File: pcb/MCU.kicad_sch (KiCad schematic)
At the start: 47 parts, among them J3 Conn_ST_STDC14, J4 Micro_SD_Card, SW1 SW_BLUE, SW2 SW_BLACK, U7 STM32U595ZJTx, Y2 16MHz

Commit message: pcb
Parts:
- removed C65, C66, C71: 100nF, Capacitor_SMD:C_0805_2012Metric_Pad1.18x1.45mm_HandSolder, symbol Device:C
- removed C67, C68, C70: 1uF, Capacitor_SMD:C_0805_2012Metric_Pad1.18x1.45mm_HandSolder, symbol Device:C
- renumbered C69 to C65, C72 to C66, C73 to C67, C74 to C68, D4 to D7, J3 to J4, J4 to J5, R37 to R42, R38 to R43, R39 to R44, R40 to R45, R41 to R46, R42 to R47, R43 to R48, R44 to R49, R45 to R50, R47 to R51, R48 to R52, R49 to R53, R50 to R54, R51 to R55, R52 to R56, U7 to U6
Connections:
- net +3V3A is gone; now on net +3V3: U6.32 (VREF+), U6.33 (VDDA)
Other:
- moved on the sheet: C65, SW2

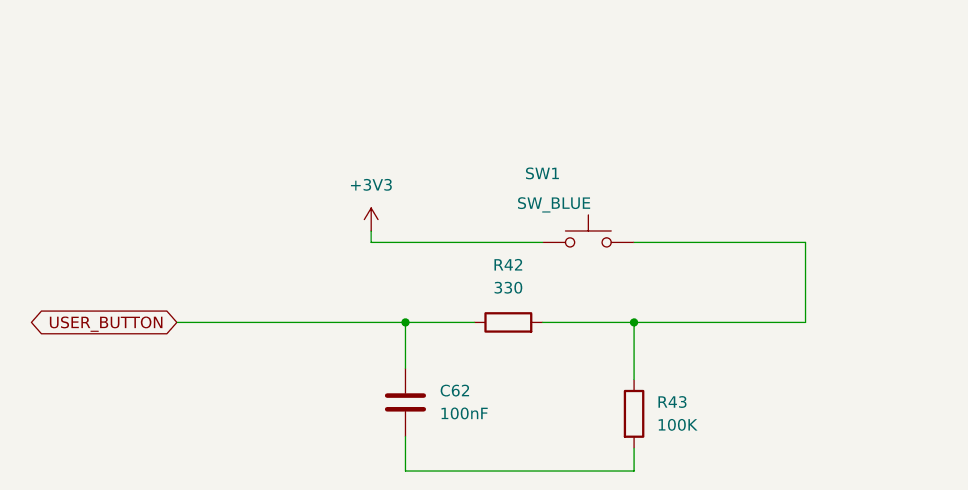
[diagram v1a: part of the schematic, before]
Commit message: pcb: simplify mcu led
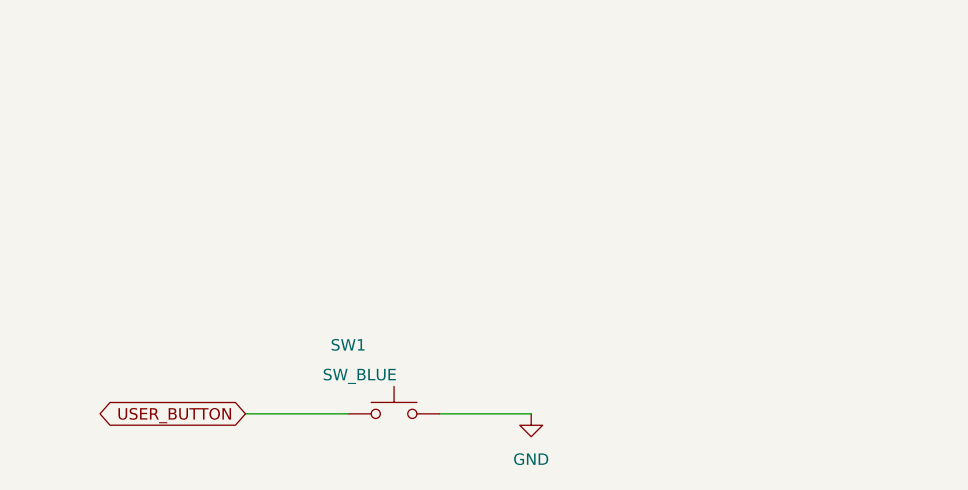
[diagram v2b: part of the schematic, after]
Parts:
- removed C62: 100nF, Capacitor_SMD:C_0805_2012Metric_Pad1.18x1.45mm_HandSolder, symbol Device:C
- removed R42: 330, Resistor_SMD:R_0805_2012Metric_Pad1.20x1.40mm_HandSolder, symbol Device:R
- removed R43: 100K, Resistor_SMD:R_0805_2012Metric_Pad1.20x1.40mm_HandSolder, symbol Device:R
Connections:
- net +3V3: no longer SW1.1
- net GND: now also SW1.2
- net USER_BUTTON: now also SW1.1
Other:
- moved on the sheet: SW1

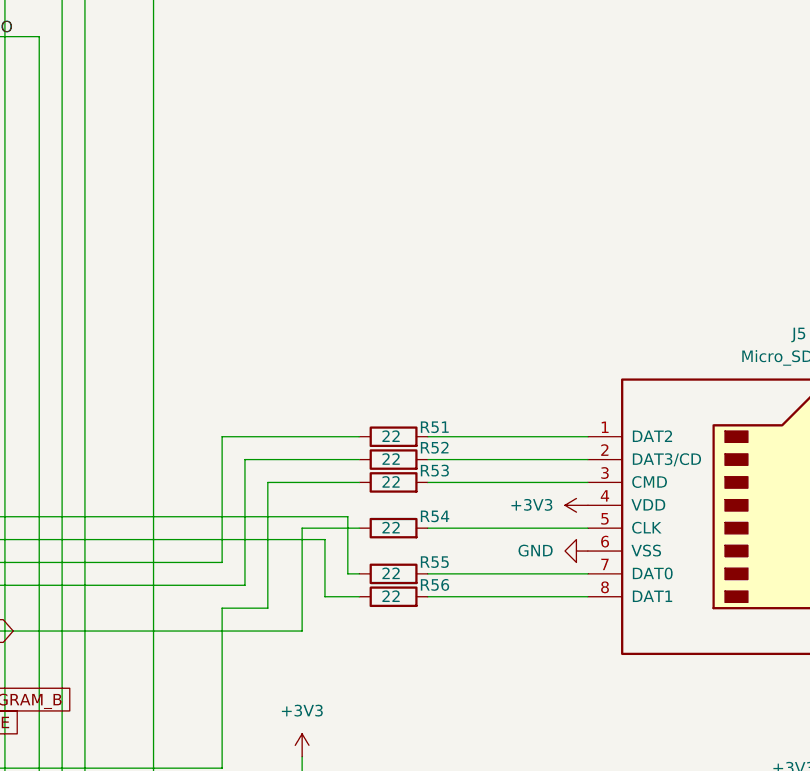
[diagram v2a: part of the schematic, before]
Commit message: add pull-up sd card
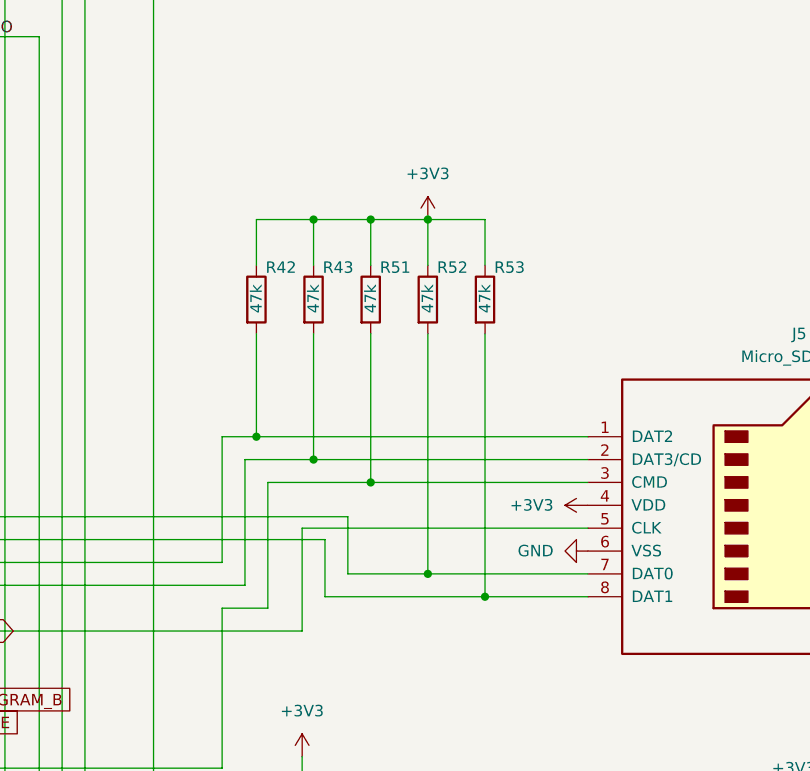
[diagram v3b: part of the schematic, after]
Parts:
- removed R54, R55, R56: 22, Resistor_SMD:R_0805_2012Metric_Pad1.20x1.40mm_HandSolder, symbol Device:R
- added R42, R43: 47k, symbol Device:R
- R51, R52, R53: value 22 -> 47k; footprint Resistor_SMD:R_0805_2012Metric_Pad1.20x1.40mm_HandSolder -> (none)
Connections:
- net +3V3: now also R51.1, R52.1, R53.1, R42.1, R43.1
- net SD_CLK: now also J5.5 (CLK)
- net SD_CMD: now also J5.3 (CMD), R51.2; no longer R53.1
- net SD_DAT0: now also J5.7 (DAT0), R52.2
- net SD_DAT1: now also J5.8 (DAT1), R53.2
- net SD_DAT2: now also J5.1 (DAT2), R42.2; no longer R51.1
- net SD_DAT3: now also J5.2 (DAT3/CD), R43.2; no longer R52.1

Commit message: pcb: wip fan out dog bone
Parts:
- R42, R43, R51, R52, R53: footprint (none) -> Resistor_SMD:R_0805_2012Metric_Pad1.20x1.40mm_HandSolder
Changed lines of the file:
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@@
 			)
 		)
-		(property "Footprint" ""
+		(property "Footprint" "Resistor_SMD:R_0805_2012Metric_Pad1.20x1.40mm_HandSolder"
 			(at 258.572 148.59 90)
 			(hide yes)
@@
 			)
 		)
-		(property "Footprint" ""
+		(property "Footprint" "Resistor_SMD:R_0805_2012Metric_Pad1.20x1.40mm_HandSolder"
 			(at 277.622 148.59 90)
 			(hide yes)
@@
 			)
 		)
-		(property "Footprint" ""
+		(property "Footprint" "Resistor_SMD:R_0805_2012Metric_Pad1.20x1.40mm_HandSolder"
 			(at 283.972 148.59 90)
 			(hide yes)
@@
 			)
 		)
-		(property "Footprint" ""
+		(property "Footprint" "Resistor_SMD:R_0805_2012Metric_Pad1.20x1.40mm_HandSolder"
 			(at 264.922 148.59 90)
 			(hide yes)
@@
 			)
 		)
-		(property "Footprint" ""
+		(property "Footprint" "Resistor_SMD:R_0805_2012Metric_Pad1.20x1.40mm_HandSolder"
 			(at 271.272 148.59 90)
 			(hide yes)

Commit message: pcb: finish vga
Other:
- note added: "spi redundancy"
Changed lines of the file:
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@@
+		)
+	)
+	(text "spi redundancy"
+		(exclude_from_sim no)
+		(at 250.698 166.624 0)
+		(effects
+			(font
+				(size 1.27 1.27)
+			)
 		)
 	)

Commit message: pcb/fpga: add user button
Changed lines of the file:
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@@
+		)
+	)
+	(label "USER_BUTTON"
+		(at 40.64 270.51 180)
+		(effects
+			(font
+				(size 1.27 1.27)
+			)
+			(justify right bottom)
 		)
 	)
@@
 		)
 	)
+	(label "USER_BUTTON"
+		(at 217.17 185.42 0)
+		(effects
+			(font
+				(size 1.27 1.27)
+			)
+			(justify left bottom)
+		)
+	)
 	(label "SD_CMD"
 		(at 218.44 200.66 0)
@@
 		)
 	)
-	(global_label "USER_BUTTON"
-		(shape bidirectional)
-		(at 40.64 270.51 180)
-		(fields_autoplaced yes)
-		(effects
-			(font
-				(size 1.27 1.27)
-			)
-			(justify right)
-		)
-		(property "Intersheetrefs" "${INTERSHEET_REFS}"
-			(at 23.4202 270.51 0)
-			(hide yes)
-			(show_name no)
-			(do_not_autoplace no)
-			(effects
-				(font
-					(size 1.27 1.27)
-				)
-				(justify right)
-			)
-		)
-	)
 	(global_label "CC1"
 		(shape bidirectional)
@@
 			(hide yes)
 			(show_name no)
-			(do_not_autoplace no)
-			(effects
-				(font
-					(size 1.27 1.27)
-				)
-				(justify left)
-			)
-		)
-	)
-	(global_label "USER_BUTTON"
-		(shape bidirectional)
-		(at 217.17 185.42 0)
-		(fields_autoplaced yes)
-		(effects
-			(font
-				(size 1.27 1.27)
-			)
-			(justify left)
-		)
-		(property "Intersheetrefs" "${INTERSHEET_REFS}"
-			(at 234.3898 185.42 0)
-			(hide yes)
-			(show_name no)
